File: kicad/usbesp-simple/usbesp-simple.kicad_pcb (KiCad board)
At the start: 2 copper layers, 10.2 x 11.4 mm, 7 parts, among them J1 USB_B_Micro, J2 Conn_01x02, J3 Conn_01x02, U1 FT230XS

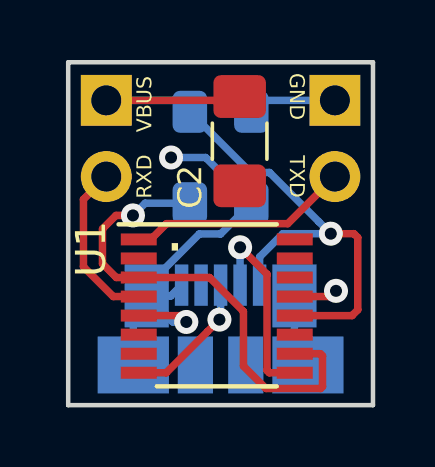
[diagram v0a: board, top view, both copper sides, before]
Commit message: migrated to single wire half duplex method
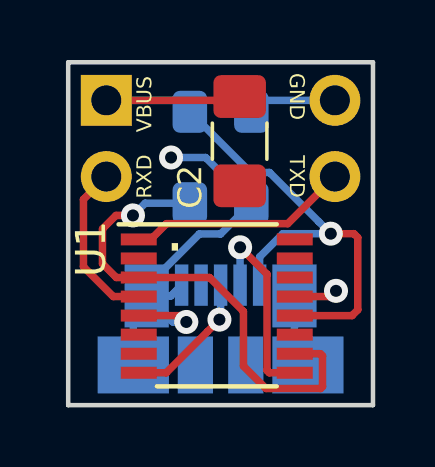
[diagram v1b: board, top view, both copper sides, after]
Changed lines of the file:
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@@
     (mod_text_size 1 1)
     (mod_text_width 0.15)
-    (pad_size 1.75 0.45)
-    (pad_drill 0)
+    (pad_size 1.7 1.7)
+    (pad_drill 1)
     (pad_to_mask_clearance 0.2)
     (aux_axis_origin 0 0)
     (visible_elements FFFFFF7F)
     (pcbplotparams
-      (layerselection 0x010fc_ffffffff)
-      (usegerberextensions false)
+      (layerselection 0x010f0_ffffffff)
+      (usegerberextensions true)
       (usegerberattributes false)
       (usegerberadvancedattributes false)
@@
       (psa4output false)
       (plotreference true)
-      (plotvalue true)
+      (plotvalue false)
       (plotinvisibletext false)
       (padsonsilk false)
-      (subtractmaskfromsilk false)
+      (subtractmaskfromsilk true)
       (outputformat 1)
       (mirror false)
-      (drillshape 1)
+      (drillshape 0)
       (scaleselection 1)
       (outputdirectory ""))
@@
       (effects (font (size 1 1) (thickness 0.15)) (justify mirror))
     )
-    (pad 1 thru_hole rect (at 0 0 180) (size 1.7 1.7) (drill 1) (layers *.Cu *.Mask)
+    (pad 1 thru_hole circle (at 0 0 180) (size 1.7 1.7) (drill 1) (layers *.Cu *.Mask)
       (net 5 GND))
     (pad 2 thru_hole oval (at 0 -2.54 180) (size 1.7 1.7) (drill 1) (layers *.Cu *.Mask)
